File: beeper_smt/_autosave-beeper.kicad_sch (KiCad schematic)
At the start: 15 parts

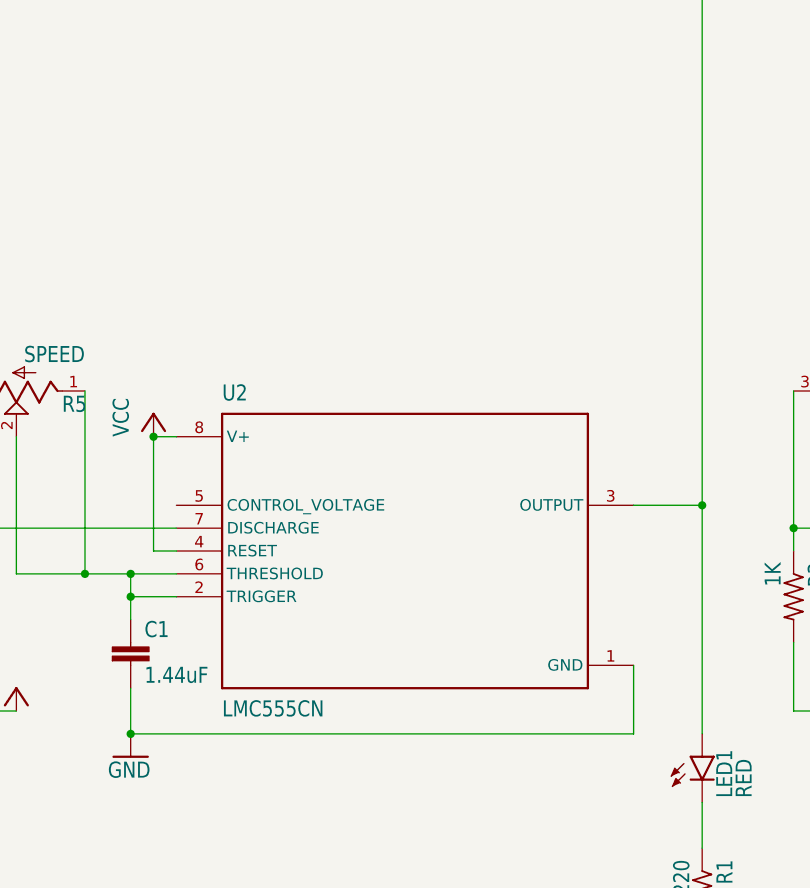
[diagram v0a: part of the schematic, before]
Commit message: add beeper_smt project
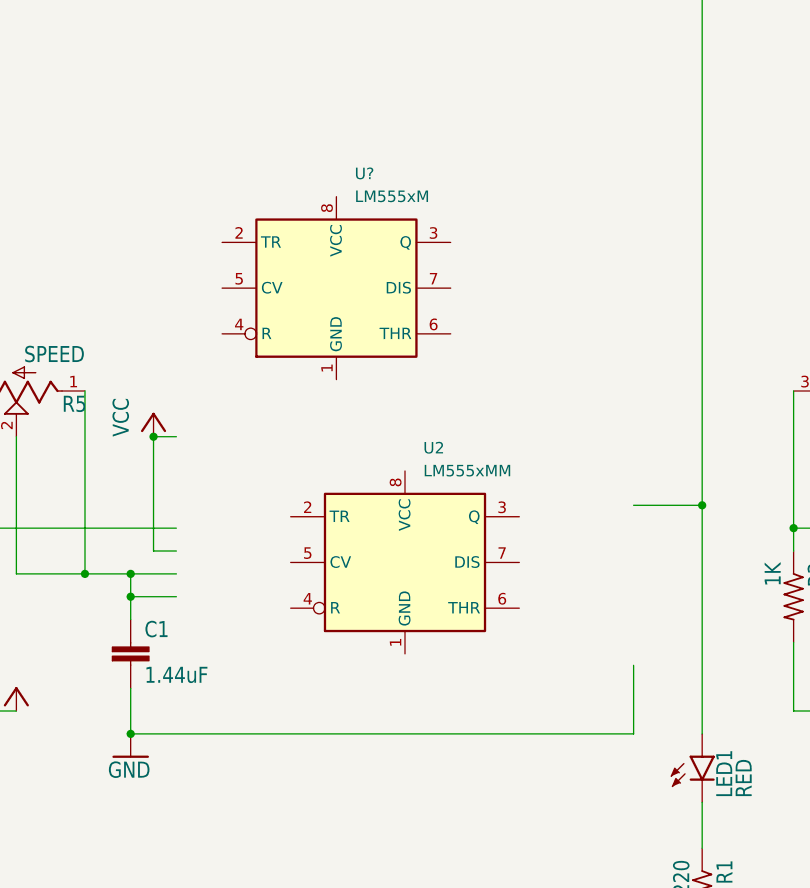
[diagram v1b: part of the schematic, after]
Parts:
- removed U2: (no value), beeper:DIP794W45P254L959H508Q8, symbol beeper-eagle-import:LMC555CN
- added U2: LM555xMM, Package_SO:VSSOP-8_3.0x3.0mm_P0.65mm, symbol Timer:LM555xMM
- added U?: LM555xM, Package_SO:SOIC-8_3.9x4.9mm_P1.27mm, symbol Timer:LM555xM
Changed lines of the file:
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@@
     (pin "1")
   )
-  (symbol (lib_id "beeper-eagle-import:GND") (at 147.32 129.54 0) (unit 1)
-    (in_bom yes) (on_board yes)
-    (property "Reference" "#GND02" (id 0) (at 147.32 129.54 0)
-      (effects (font (size 1.27 1.27)) hide)
-    )
-    (property "Value" "GND" (id 1) (at 144.78 132.08 0)
-      (effects (font (size 1.778 1.5113)) (justify left bottom))
-    )
-    (property "Footprint" "beeper:" (id 2) (at 147.32 129.54 0)
-      (effects (font (size 1.27 1.27)) hide)
-    )
-    (property "Datasheet" "" (id 3) (at 147.32 129.54 0)
-      (effects (font (size 1.27 1.27)) hide)
-    )
-    (pin "1")
-  )
-  (symbol (lib_id "beeper-eagle-import:VCC") (at 45.72 157.48 0) (unit 1)
-    (in_bom yes) (on_board yes)
-    (property "Reference" "#P+7" (id 0) (at 45.72 157.48 0)
-      (effects (font (size 1.27 1.27)) hide)
-    )
-    (property "Value" "VCC" (id 1) (at 43.18 160.02 90)
-      (effects (font (size 1.778 1.5113)) (justify left bottom))
-    )
-    (property "Footprint" "beeper:" (id 2) (at 45.72 157.48 0)
-      (effects (font (size 1.27 1.27)) hide)
-    )
-    (property "Datasheet" "" (id 3) (at 45.72 157.48 0)
-      (effects (font (size 1.27 1.27)) hide)
-    )
-    (pin "1")
-  )
-  (symbol (lib_id "beeper-eagle-import:LMC555CN") (at 78.74 106.68 0) (unit 1)
-    (in_bom yes) (on_board yes)
-    (property "Reference" "U2" (id 0) (at 58.42 90.17 0)
-      (effects (font (size 1.778 1.5113)) (justify left bottom))
-    )
-    (property "Value" "LMC555CN" (id 1) (at 58.42 123.19 0)
-      (effects (font (size 1.778 1.5113)) (justify left top))
-    )
-    (property "Footprint" "beeper:DIP794W45P254L959H508Q8" (id 2) (at 78.74 106.68 0)
-      (effects (font (size 1.27 1.27)) hide)
-    )
-    (property "Datasheet" "" (id 3) (at 78.74 106.68 0)
-      (effects (font (size 1.27 1.27)) hide)
-    )
-    (property "Value" "" (id 4) (at 78.74 106.68 0)
-      (effects (font (size 1.778 1.5113)) (justify left bottom) hide)
-    )
-    (pin "1")
+  (symbol (lib_id "Timer:LM555xM") (at 71.12 77.47 0) (unit 1)
+    (in_bom yes) (on_board yes) (fields_autoplaced)
+    (property "Reference" "U?" (id 0) (at 73.1394 64.77 0)
+      (effects (font (size 1.27 1.27)) (justify left))
+    )
+    (property "Value" "LM555xM" (id 1) (at 73.1394 67.31 0)
+      (effects (font (size 1.27 1.27)) (justify left))
+    )
+    (property "Footprint" "Package_SO:SOIC-8_3.9x4.9mm_P1.27mm" (id 2) (at 92.71 87.63 0)
+      (effects (font (size 1.27 1.27)) hide)
+    )
+    (property "Datasheet" "http://www.ti.com/lit/ds/symlink/lm555.pdf" (id 3) (at 92.71 87.63 0)
+      (effects (font (size 1.27 1.27)) hide)
+    )
+    (pin "1")
+    (pin "8")
     (pin "2")
     (pin "3")
@@
     (pin "6")
     (pin "7")
-    (pin "8")
+  )
+  (symbol (lib_id "beeper-eagle-import:GND") (at 147.32 129.54 0) (unit 1)
+    (in_bom yes) (on_board yes)
+    (property "Reference" "#GND02" (id 0) (at 147.32 129.54 0)
+      (effects (font (size 1.27 1.27)) hide)
+    )
+    (property "Value" "GND" (id 1) (at 144.78 132.08 0)
+      (effects (font (size 1.778 1.5113)) (justify left bottom))
+    )
+    (property "Footprint" "beeper:" (id 2) (at 147.32 129.54 0)
+      (effects (font (size 1.27 1.27)) hide)
+    )
+    (property "Datasheet" "" (id 3) (at 147.32 129.54 0)
+      (effects (font (size 1.27 1.27)) hide)
+    )
+    (pin "1")
+  )
+  (symbol (lib_id "beeper-eagle-import:VCC") (at 45.72 157.48 0) (unit 1)
+    (in_bom yes) (on_board yes)
+    (property "Reference" "#P+7" (id 0) (at 45.72 157.48 0)
+      (effects (font (size 1.27 1.27)) hide)
+    )
+    (property "Value" "VCC" (id 1) (at 43.18 160.02 90)
+      (effects (font (size 1.778 1.5113)) (justify left bottom))
+    )
+    (property "Footprint" "beeper:" (id 2) (at 45.72 157.48 0)
+      (effects (font (size 1.27 1.27)) hide)
+    )
+    (property "Datasheet" "" (id 3) (at 45.72 157.48 0)
+      (effects (font (size 1.27 1.27)) hide)
+    )
+    (pin "1")
   )
   (symbol (lib_id "beeper-eagle-import:R-US_0204{slash}7") (at 236.22 93.98 90) (unit 1)
@@
     (pin "1")
   )
+  (symbol (lib_id "Timer:LM555xMM") (at 78.74 107.95 0) (unit 1)
+    (in_bom yes) (on_board yes) (fields_autoplaced)
+    (property "Reference" "U2" (id 0) (at 80.7594 95.25 0)
+      (effects (font (size 1.27 1.27)) (justify left))
+    )
+    (property "Value" "LM555xMM" (id 1) (at 80.7594 97.79 0)
+      (effects (font (size 1.27 1.27)) (justify left))
+    )
+    (property "Footprint" "Package_SO:VSSOP-8_3.0x3.0mm_P0.65mm" (id 2) (at 95.25 118.11 0)
+      (effects (font (size 1.27 1.27)) hide)
+    )
+    (property "Datasheet" "http://www.ti.com/lit/ds/symlink/lm555.pdf" (id 3) (at 100.33 118.11 0)
+      (effects (font (size 1.27 1.27)) hide)
+    )
+    (pin "1")
+    (pin "8")
+    (pin "2")
+    (pin "3")
+    (pin "4")
+    (pin "5")
+    (pin "6")
+    (pin "7")
+  )
   (symbol (lib_id "beeper-eagle-import:C2,5-3") (at 147.32 116.84 0) (unit 1)
     (in_bom yes) (on_board yes)
@@
       (reference "U1") (unit 1) (value "CD4011BE") (footprint "beeper:DIP794W45P254L1969H508Q14")
     )
-    (path "/392e7667-7f98-46a5-879e-1e0103ce0532"
-      (reference "U2") (unit 1) (value "LMC555CN") (footprint "beeper:DIP794W45P254L959H508Q8")
+    (path "/afadbfc3-4ee9-4118-9be5-4dab86921067"
+      (reference "U2") (unit 1) (value "LM555xMM") (footprint "Package_SO:VSSOP-8_3.0x3.0mm_P0.65mm")
     )
     (path "/662796c8-779e-44ba-aace-76cac3066642"
       (reference "U3") (unit 1) (value "LMC555CN") (footprint "beeper:DIP794W45P254L959H508Q8")
     )
+    (path "/2579b023-ed9b-4b37-b77c-34f66d593412"
+      (reference "U?") (unit 1) (value "LM555xM") (footprint "Package_SO:SOIC-8_3.9x4.9mm_P1.27mm")
+    )
     (path "/c969034b-b876-43ca-aa04-23f9c9cdd578"
